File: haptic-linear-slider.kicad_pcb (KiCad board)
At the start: 2 copper layers, 130.5 x 33.8 mm, 78 parts, among them IC1 DIO54335TST6, IC2 TLV61048DBVR, J1 SWD, J2 USB_C_Receptacle_USB2.0_16P, J3 TBC05-02-1-G-G, J4 EXT_CTRL, SW1 SW_Reset, SW2 SW_Boot, U1 RP2354A, U2 PSM01-081A-103B2, U3 DRV8876PWPR, U4 USBLC6-2SC6, Y1 ABM8-272-T3

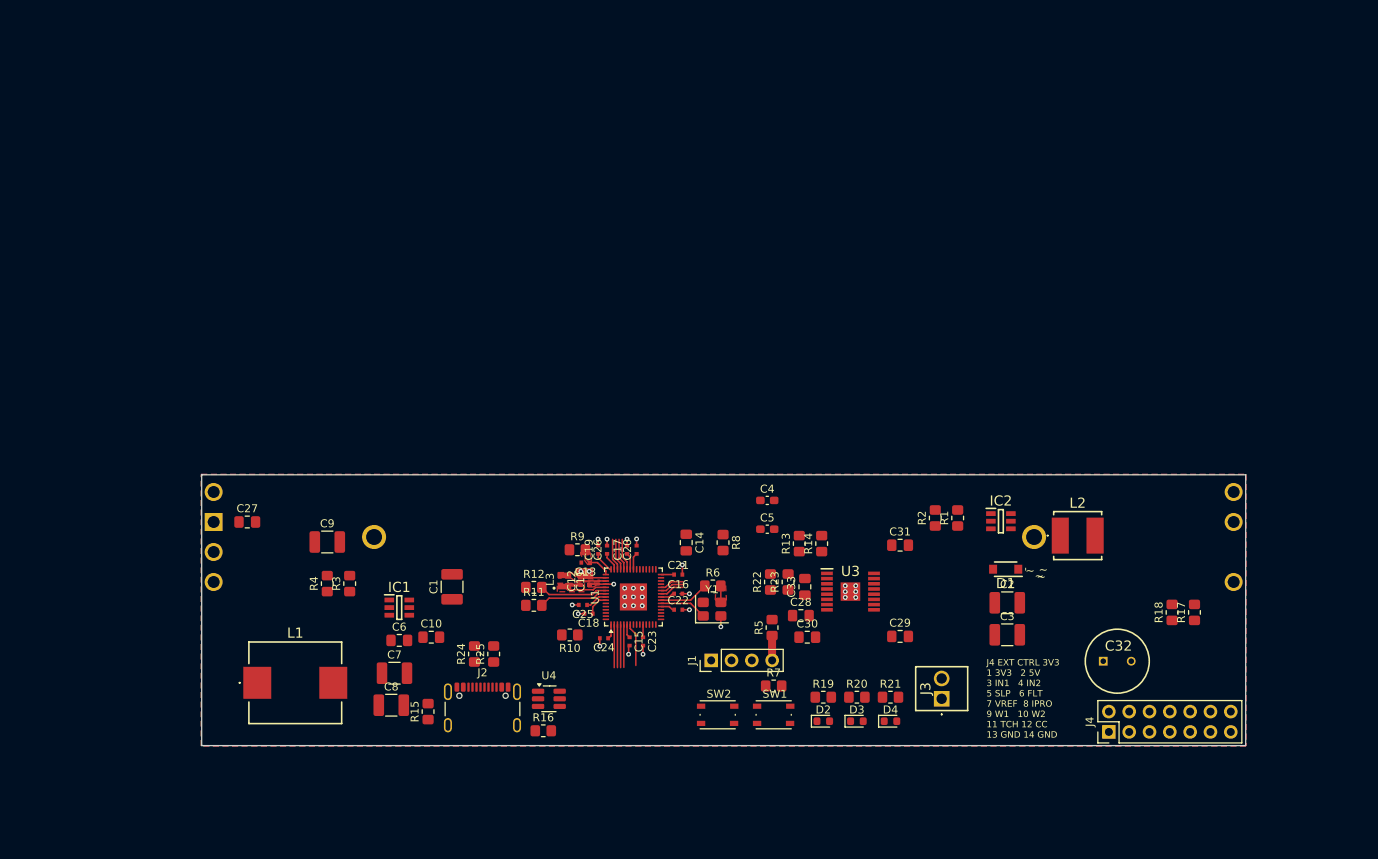
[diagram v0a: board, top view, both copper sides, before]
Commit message: Moved pin on micro for better routing
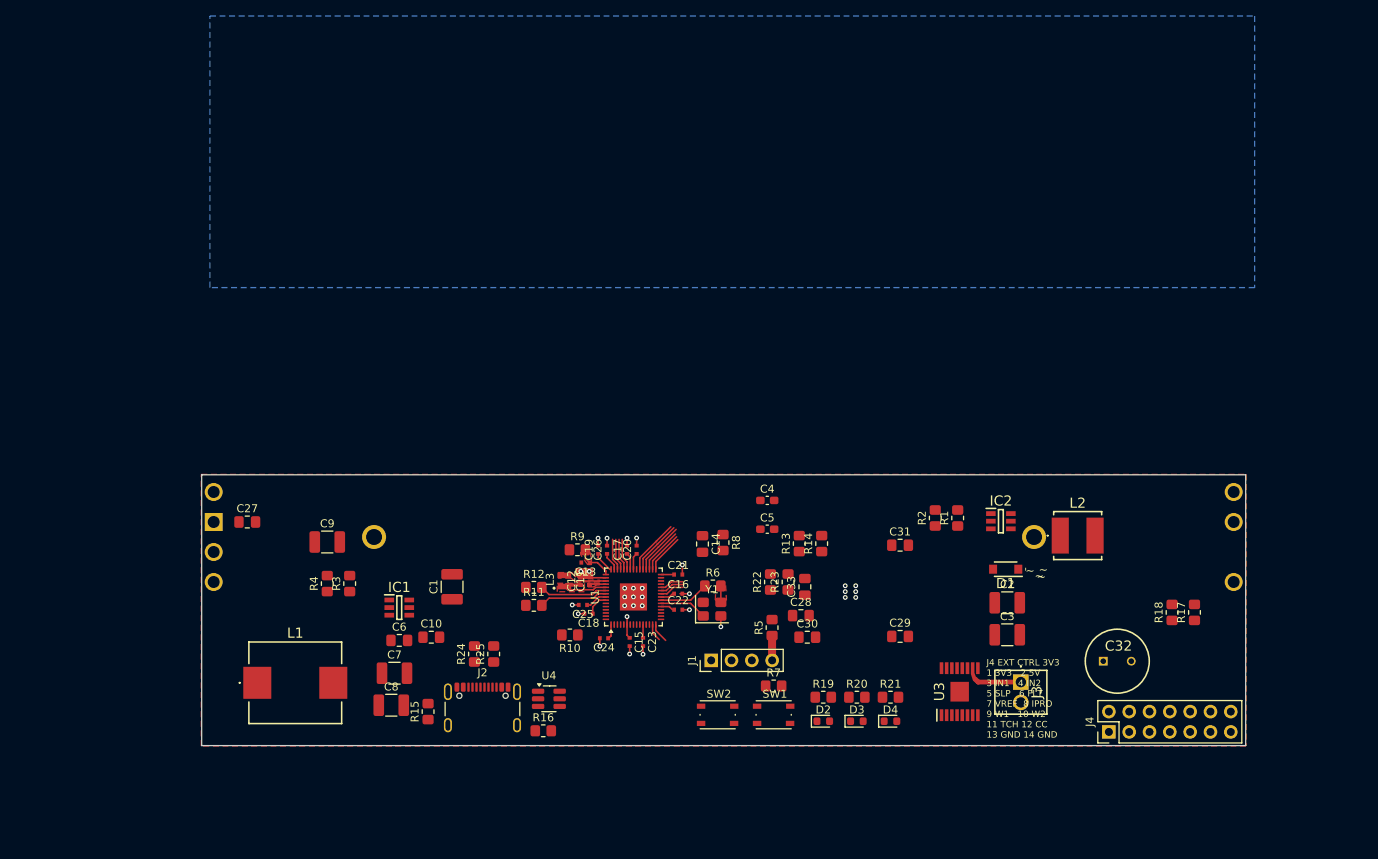
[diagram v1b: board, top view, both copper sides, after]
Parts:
- moved U3 18.5 mm to (304.6, 226.7), turned to 90 degrees
- moved J3 10.1 mm to (312.3, 225.5), turned to -90 degrees
- moved C14 2.04 mm to (272.5, 208.2)
- moved C15 0.07 mm to (263.4, 220.5)
- moved C23 0.07 mm to (265.1, 220.5)
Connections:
- U1 pad 14: unconnected-(U1-GPIO10-Pad14) -> /STATUS_LED1
- U1 pad 15: unconnected-(U1-GPIO11-Pad15) -> /STATUS_LED2
- U1 pad 2: /MOTOR_IN1 -> unconnected-(U1-GPIO0-Pad2)
- U1 pad 3: /MOTOR_IN2 -> unconnected-(U1-GPIO1-Pad3)
- U1 pad 31: unconnected-(U1-GPIO19-Pad31) -> /MOTOR_IN1
- U1 pad 32: unconnected-(U1-GPIO20-Pad32) -> /MOTOR_IN2
- U1 pad 33: unconnected-(U1-GPIO21-Pad33) -> /MOTOR_~{SLEEP}
- U1 pad 34: /TOUCH_SENSE -> /MOTOR_~{FAULT}
- U1 pad 35: unconnected-(U1-GPIO23-Pad35) -> /MOTOR_VREF_PWM
- U1 pad 36: /STATUS_LED1 -> /TOUCH_SENSE
- U1 pad 37: /STATUS_LED2 -> unconnected-(U1-GPIO25-Pad37)
- U1 pad 4: /MOTOR_~{SLEEP} -> unconnected-(U1-GPIO2-Pad4)
- U1 pad 5: /MOTOR_~{FAULT} -> unconnected-(U1-GPIO3-Pad5)
- U1 pad 7: /MOTOR_VREF_PWM -> unconnected-(U1-GPIO4-Pad7)
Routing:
- net /TOUCH_SENSE: track 0.00 -> 7.06 mm
- net Net-(U3-OUT2): track 0.00 -> 6.46 mm
- net /STATUS_LED2: track 0.00 -> 2.49 mm
- net /STATUS_LED1: track 0.00 -> 2.22 mm
- net /MOTOR_VREF_PWM: track 5.40 -> 6.93 mm
- net +1V1: track 12.9 -> 14.1 mm, vias 0 -> 1
- net /MOTOR_~{FAULT}: track 5.35 -> 6.54 mm
- net +3V3: track 22.2 -> 21.2 mm, vias 1 -> 0
- net /MOTOR_IN1: track 5.38 -> 4.86 mm

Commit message: Condensatori
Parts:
- added C34: 10n, Capacitor_SMD:C_0805_2012Metric_Pad1.18x1.45mm_HandSolder, F.Cu at (292.7, 202.5)
- added R26: 20k, Resistor_SMD:R_0805_2012Metric_Pad1.20x1.40mm_HandSolder, F.Cu at (292.7, 205.5)
- moved C32 140.1 mm to (199.9, 155.2)
- moved U3 127.8 mm to (193.9, 162.8)
- moved J3 126.8 mm to (202.5, 162.1)
- moved C29 119.5 mm to (195.6, 157.0)
- moved C31 117.0 mm to (191.8, 157.7), turned to 180 degrees
- moved C30 111.1 mm to (195.6, 154.9), turned to 180 degrees
- moved R13 100.9 mm to (191.6, 169.0)
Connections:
- U3 pad 7: GND -> Net-(U3-IMODE)
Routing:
- net GND: track 18.6 -> 3.61 mm, vias 30 -> 0
- net +10V: track 0.00 -> 9.16 mm
- net /MOTOR_~{SLEEP}: track 5.77 -> 12.0 mm
- net Net-(U3-OUT1): track 0.00 -> 5.96 mm
- net /MOTOR_IN2: track 5.31 -> 10.3 mm
- net Net-(U3-CPL): track 0.00 -> 3.69 mm
- net /MOTOR_~{FAULT}: track 6.54 -> 10.1 mm
- net Net-(U3-VCP): track 0.00 -> 3.03 mm
- net /MOTOR_IN1: track 4.86 -> 7.77 mm
- net Net-(U3-CPH): track 0.00 -> 2.48 mm
- net (no net): vias 0 -> 10

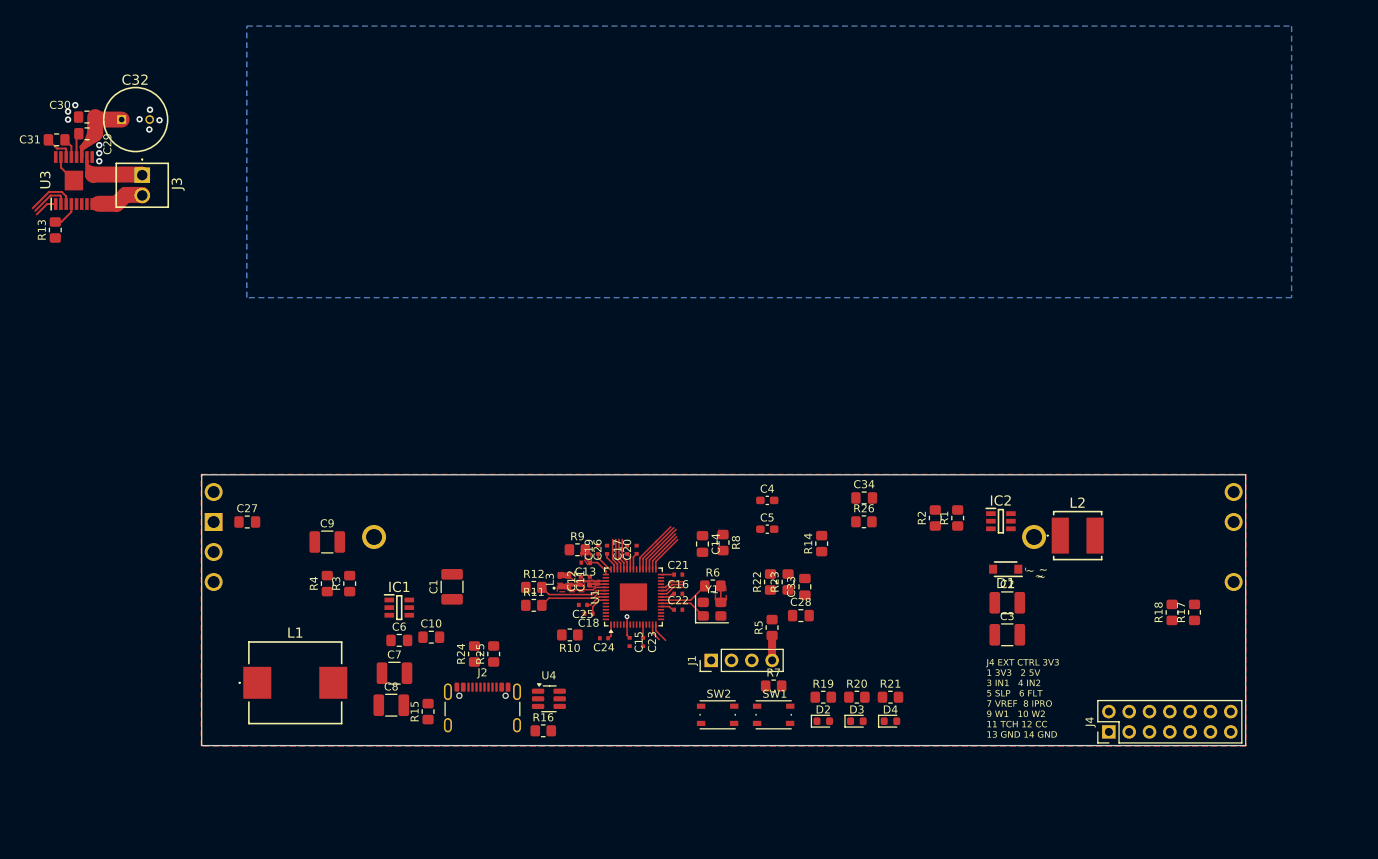
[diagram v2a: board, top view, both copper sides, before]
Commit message: Ho fatto il layout di USB, convertitori DCDC e ponte H. Il layout della USB non so come si faccia e l'ho fatto a caso. Ho cambiato il piano superiore da GND a 3V3. Buonanotte Gengis.
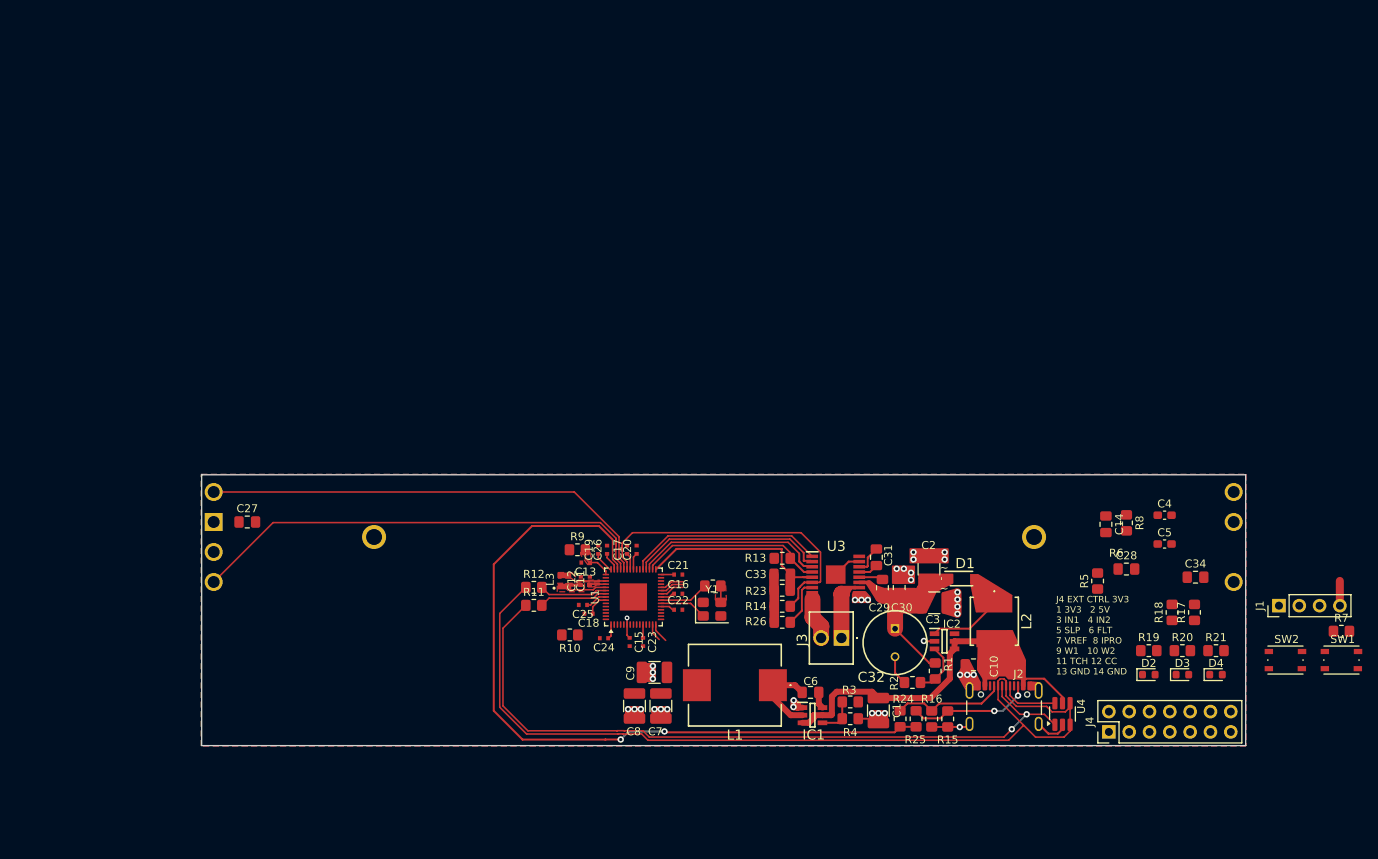
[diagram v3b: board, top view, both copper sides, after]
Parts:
- removed R22: 10k, Resistor_SMD:R_0805_2012Metric_Pad1.20x1.40mm_HandSolder
- moved C30 117.3 mm to (297.1, 213.7), turned to 90 degrees
- moved C32 115.7 mm to (296.6, 218.8), turned to -90 degrees
- moved C31 115.0 mm to (294.2, 209.9), turned to 90 degrees
- moved C29 114.5 mm to (295.0, 213.7), turned to -90 degrees
- moved U3 107.2 mm to (289.2, 212.1), turned to 0 degrees
- moved J3 104.8 mm to (289.9, 220.0), turned to 180 degrees
- moved R13 99.7 mm to (282.5, 210.0), turned to 0 degrees
- moved J1 71.3 mm to (344.6, 216.0)
- moved R7 71.3 mm to (352.4, 219.2)
- moved SW1 71.3 mm to (352.4, 222.8)
- moved SW2 71.3 mm to (345.4, 222.8)
- moved C10 67.9 mm to (306.4, 223.3), turned to 180 degrees
- moved R4 67.5 mm to (291.0, 230.1), turned to 0 degrees
- moved J2 65.2 mm to (310.2, 229.7)
- moved R15 65.0 mm to (303.2, 230.1), turned to -90 degrees
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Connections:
- C33 pad 1: Net-(U3-VREF) -> /MOTOR_VREF_PWM
- R23 pad 1: Net-(U3-VREF) -> /MOTOR_VREF_PWM
- U1 pad 31: /MOTOR_IN1 -> /MOTOR_VREF_PWM
- U1 pad 32: /MOTOR_IN2 -> /MOTOR_~{FAULT}
- U1 pad 34: /MOTOR_~{FAULT} -> /MOTOR_IN2
- U1 pad 35: /MOTOR_VREF_PWM -> /MOTOR_IN1
- U1 pad 40: /POT_WIPER1 -> /MOTOR_IPROPI
- U1 pad 41: /POT_WIPER2 -> /POT_WIPER1
- U1 pad 42: /CC_SENSE -> /POT_WIPER2
- U1 pad 43: /MOTOR_IPROPI -> /CC_SENSE
- U3 pad 5: Net-(U3-VREF) -> /MOTOR_VREF_PWM
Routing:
- net /USB_D-: track 0.00 -> 114.8 mm
- net /USB_D+: track 0.00 -> 98.6 mm, vias 0 -> 2
- net /CC_SENSE: track 4.00 -> 94.9 mm, vias 0 -> 2
- net /POT_WIPER2: track 4.00 -> 59.1 mm
- net /POT_WIPER1: track 4.00 -> 57.3 mm
- net GND: track 3.61 -> 56.8 mm, vias 0 -> 34
- net +5V: track 0.00 -> 42.3 mm
- net /MOTOR_IPROPI: track 4.00 -> 39.5 mm
- net /MOTOR_VREF_PWM: track 6.93 -> 26.4 mm
- net /MOTOR_IN1: track 7.77 -> 24.6 mm
- net /CC2: track 0.00 -> 15.5 mm, vias 0 -> 2
- net +10V: track 9.16 -> 23.5 mm
- net /MOTOR_IN2: track 10.3 -> 24.6 mm
- net /CC1: track 0.00 -> 14.2 mm
- net /MOTOR_~{FAULT}: track 10.1 -> 24.0 mm
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- removed copper zone on F.Cu, net GND
